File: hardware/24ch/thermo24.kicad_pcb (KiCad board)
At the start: 4 copper layers, 170 x 145 mm, 462 parts, among them J101 TC CH1-4, J102 TC CH5-8, J201 TC CH9-12, J202 TC CH13-16, J301 TC CH17-20, J302 TC CH21-24, J401 ENGINE REF FEED/SENSE, J501 AVR ISP, J502 LCD 20x4 HEADER, J601 24V IN, J701 TRIP C-NO-NC, J702 ALM C-NO-NC, J703 RS485 A B GND, K701 G6K-2F-Y DC5, K702 G6K-2F-Y DC5, Q401 2N7002, Q402 MMBT3906, Q701 2N7002, Q702 2N7002, SW501 UP, SW502 DOWN, SW503 SET, SW504 ESC, SW505 ACK, U101 AD7124-8BCPZ, U102 ADT7310TRZ, U103 ADT7310TRZ, U201 AD7124-8BCPZ, U202 ADT7310TRZ, U203 ADT7310TRZ, U301 AD7124-8BCPZ, U302 ADT7310TRZ, U303 ADT7310TRZ, U401 B0505S-1WR2, U402 LP2985IM5X-3.3, U403 ISO7761DWR, U404 ISO7761DWR, U405 ISO7761DWR, U406 REF3030AIDBZR, U407 MCP6001T-I/OT, U408 TLV7031DBVR, U409 TL431, U501 ATmega1284P-AU, U601 LM5164DDAR, U703 ADM2587EBRWZ, Y501 8MHz

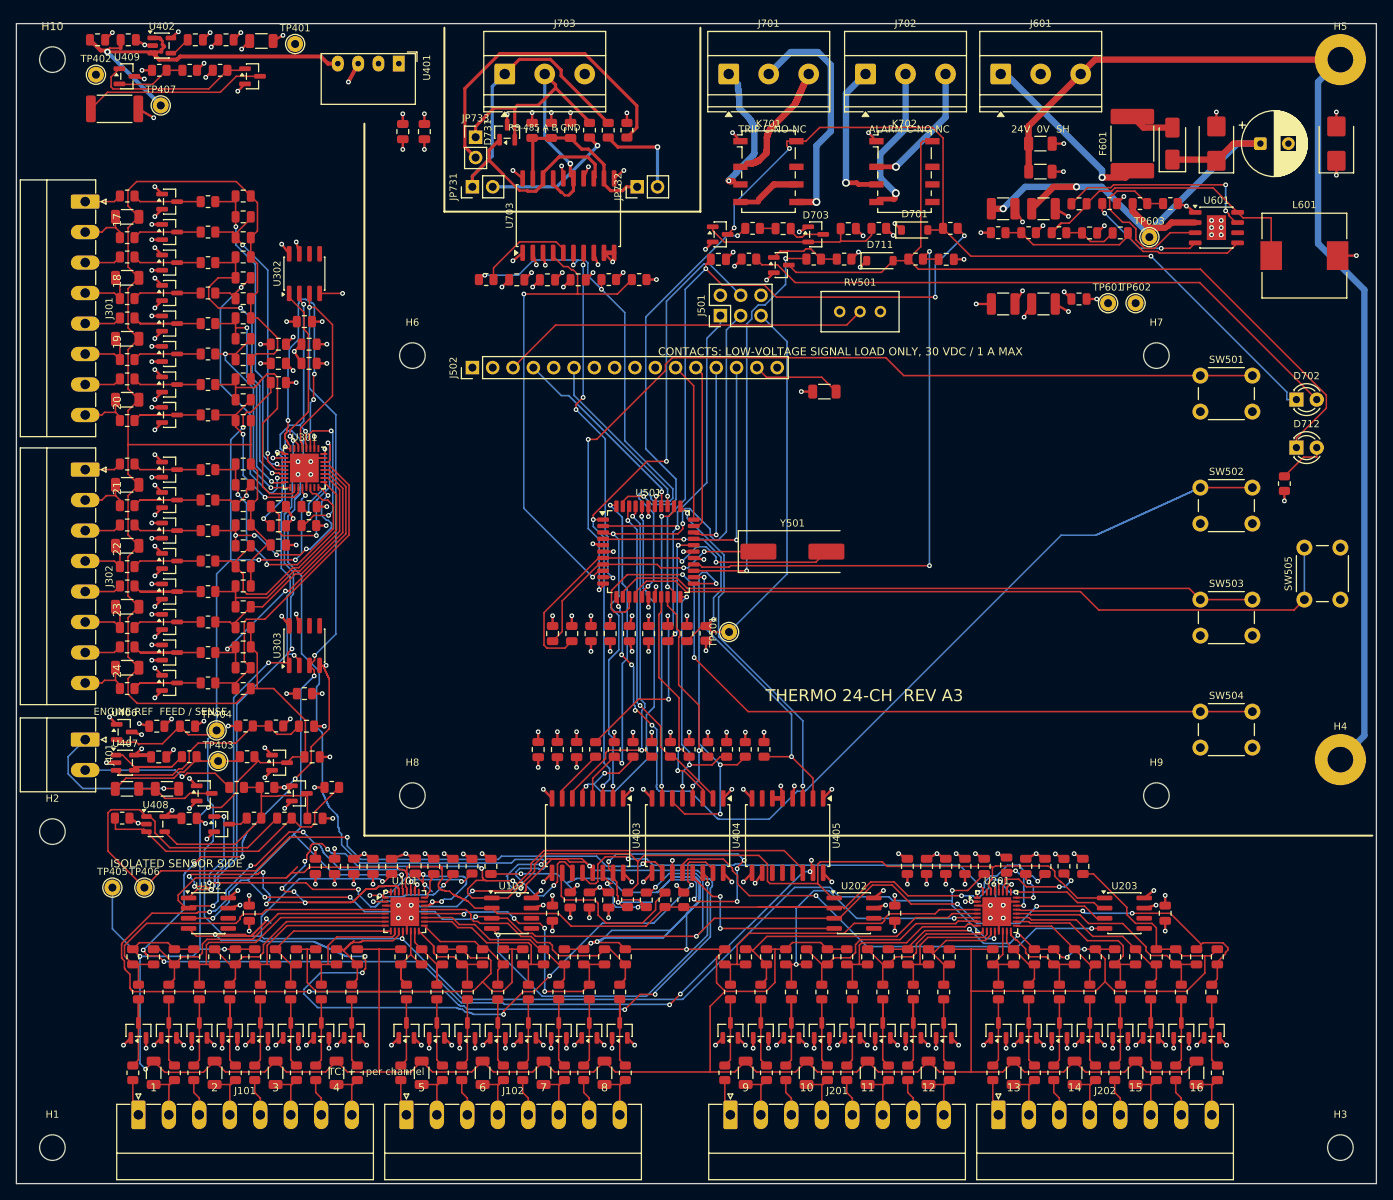
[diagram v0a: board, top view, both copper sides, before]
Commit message: 24-ch board routed: DRC 0 violations, 0 unconnected, 0 footprint errors
Last two connections finished (TC21 pair re-assigned, TC21_PA and two
CS_CJ5_ISO pieces on In2.Cu - 0033 D4). rules.py full: outer pours, NORI
pad-to-track 0.2 mm on pads, relay_area only for contact nets. finish.py
gains nori (push tracks off pads), dangling (delete router stubs, each
checked by DRC on a copy); maze.py can use In2.Cu and starts from vias.
pcb sync applied (C8545, C28260; 0 pad changes). Report:
output/drc-synced.rpt (0/0/0, schematic parity).

Co-Authored-By: Claude Opus 5.5 <noreply@anthropic.com>
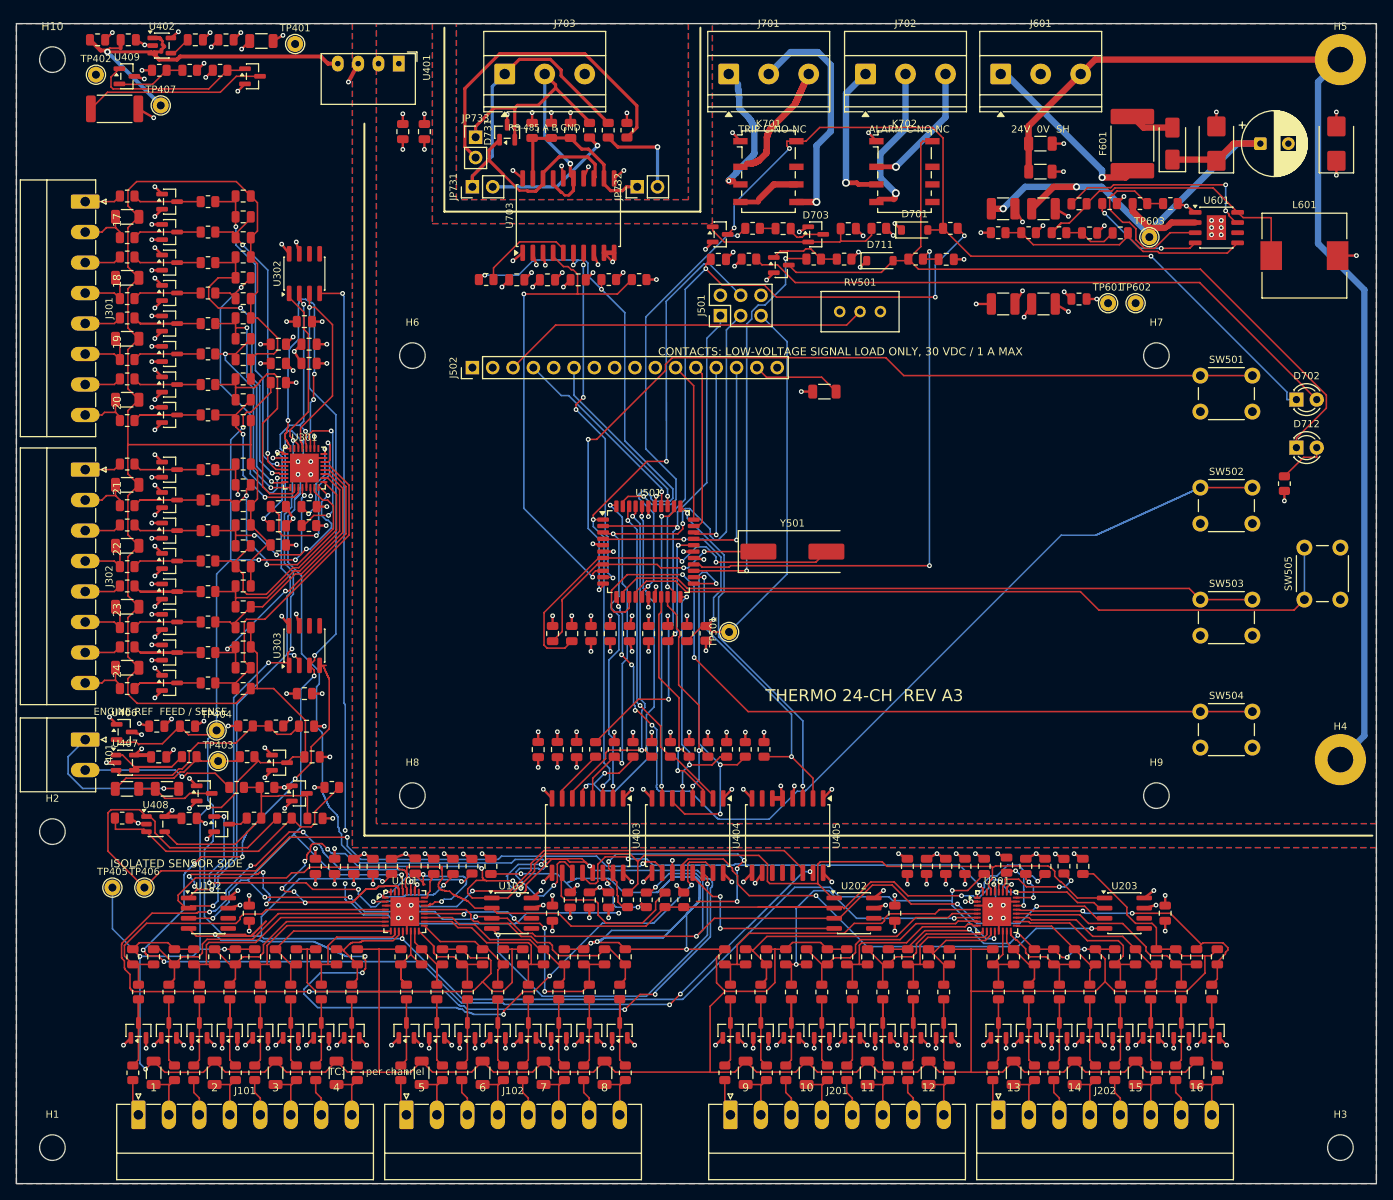
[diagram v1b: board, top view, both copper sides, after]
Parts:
- C604: value 2.2n -> 2.2n C0G
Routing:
- net CS_CJ5_ISO: track 4.41 -> 125.5 mm, vias 2 -> 5
- net TC21_NA: track 6.29 -> 32.6 mm, vias 1 -> 2
- net TC21_PA: track 33.9 -> 17.7 mm
- net /ISOLATION_1/SCLK_ISO_RAW: track 45.0 -> 35.3 mm, vias 6 -> 4
- net SCLK_ISO: track 284.5 -> 280.0 mm, vias 18 -> 16
- net /ISOLATION_1/DIN_ISO_RAW: track 13.4 -> 9.78 mm
- net /BANK_A_2/REFOUT_A: track 20.4 -> 18.0 mm, vias 4 -> 2
- net DOUT_ISO: track 240.9 -> 238.9 mm
- net TC4_NA: track 17.1 -> 15.3 mm
- net /BANK_A_2/REGCAPD_A: track 12.9 -> 11.3 mm, vias 3 -> 2
- net CS_CJ6_ISO: track 144.2 -> 142.8 mm, vias 10 -> 8
- net REFTEST_ISO: track 92.7 -> 91.4 mm
- net CS_CJ1_ISO: track 113.5 -> 112.4 mm, vias 7 -> 6
- net /BANK_C_2/TC22_PA: vias 5 -> 4
- added copper zone on B.Cu, net /OUTPUTS/GND_RS485
- added copper zone on F.Cu, net /OUTPUTS/GND_RS485
- added copper zone on B.Cu, net GND
- added copper zone on F.Cu, net GND
- added copper zone on B.Cu, net GND_ISO
- added copper zone on F.Cu, net GND_ISO

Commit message: 24-ch: exposed-pad vias off the paste windows (I-110)
AD7124 x3: vias on the gap cross of the 4 paste squares (U301 4, U101 2,
U201 2); CS_ADC3_ISO and DIN_ISO moved on B.Cu to make room. LM5164: 3 vias
on its only drill-wide gap. fanout.py/rules.py generate the same. DRC with
schematic parity 0/0/0 (output/drc-ep.rpt).

Co-Authored-By: Claude Opus 5.5 <noreply@anthropic.com>
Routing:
- net DIN_ISO: track 266.8 -> 267.5 mm
- net GND_ISO: vias 124 -> 120
- net GND: vias 55 -> 52
